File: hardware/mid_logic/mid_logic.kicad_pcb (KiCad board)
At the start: 4 copper layers, 52 x 52 mm, 52 parts, among them J2 J_STK_A, J3 J_STK_B, J4 RS485 A/B/GND, J5 Feld: 4 Reed, J6 Haubenkontakt, J7 USB-C, Q2 BC847, SW1 RESET, SW2 BOOT, U1 ESP32-S3-WROOM-1-N16R8, U2 MAX3485, U3 PCF8575, U4 PhotoMOS 60V, U5 USBLC6-2SC6

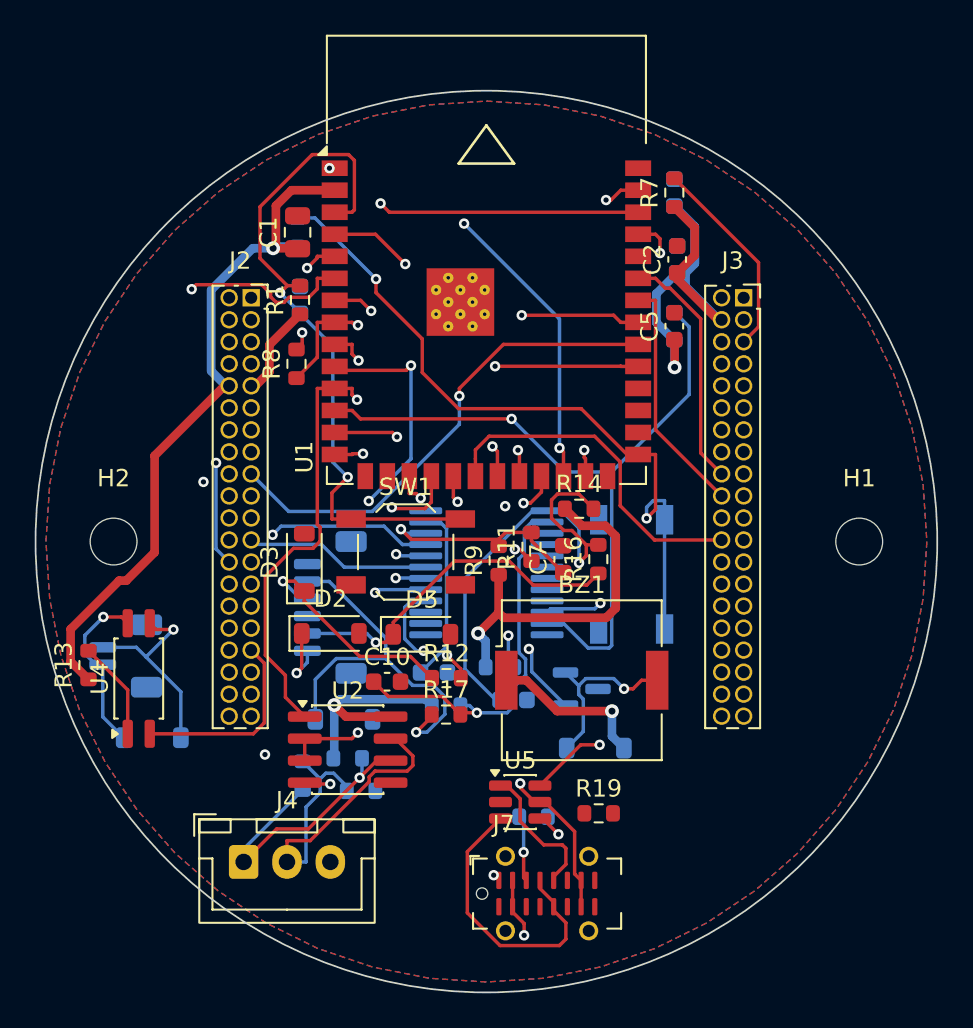
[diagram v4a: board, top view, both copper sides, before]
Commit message: docs/16: Anleitung fuer die letzten Handgriffe in KiCad
Was der Autorouter uebrig laesst, ist wenig und immer dasselbe Muster: Pads,
die zwischen anderen Bauteilen eingeklemmt sind. Die Anleitung nennt die
Tastenkuerzel (X fuer Bahn, V fuer Lagenwechsel mit Via, B fuer Zonen
fuellen), den aktuellen Stand je Board als Anhaltspunkt und die
Reihenfolge danach - Zonen fuellen VOR der DRC, sonst sucht man Fehler, die
keine sind.

Dazu zwei Warnungen: keine Bauteile verschieben, die Positionen kommen aus
gen_layouts.py und gehen beim naechsten Neuerzeugen verloren. Und die Regeln
nicht lockern - wenn die DRC meckert, ist die Bahn falsch.

Co-Authored-By: Claude Opus 5 (1M context) <noreply@anthropic.com>
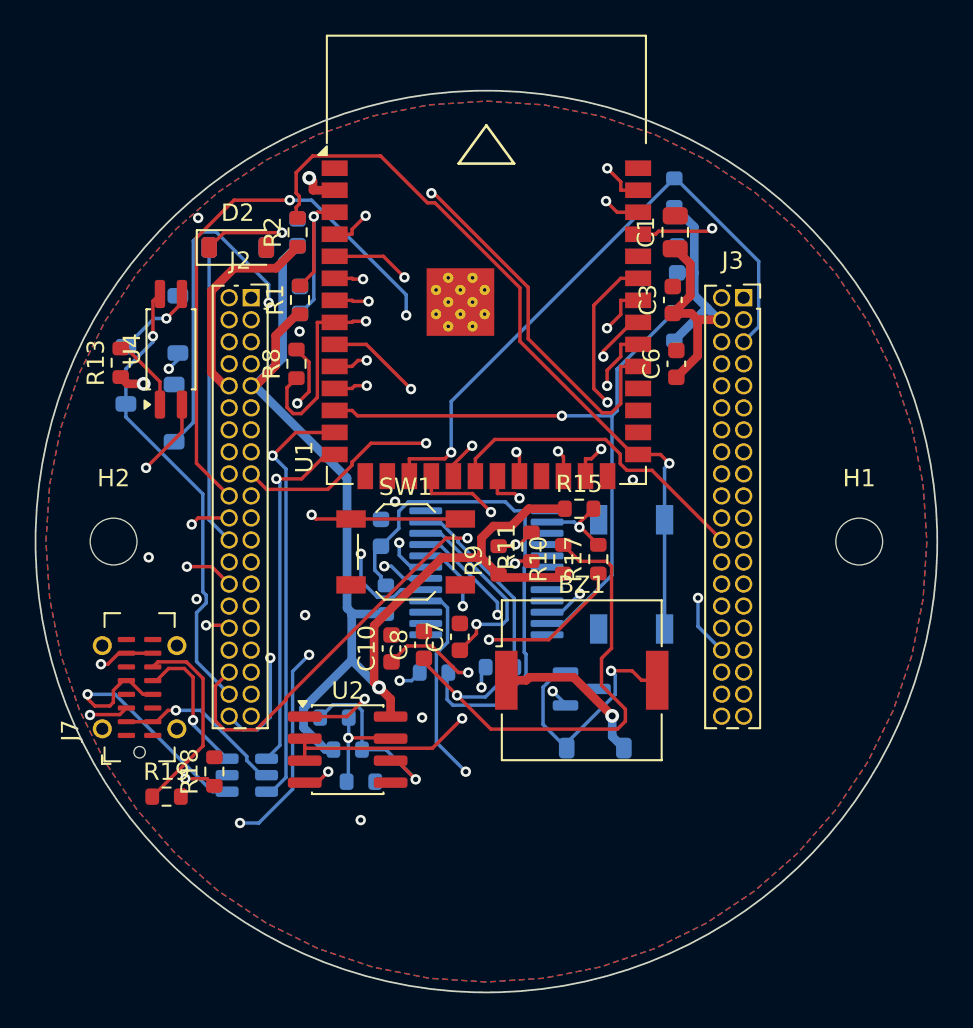
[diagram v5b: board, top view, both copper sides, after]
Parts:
- removed J4: RS485 A/B/GND, JST_XH_B3B-XH-A_1x03_P2.50mm_Vertical
- removed J5: Feld: 4 Reed, JST_SH_BM06B-SRSS-TB_1x06-1MP_P1.00mm_Vertical
- removed J6: Haubenkontakt, JST_SH_BM02B-SRSS-TB_1x02-1MP_P1.00mm_Vertical
- C2, C5, D3, D5, R12, R14, R16, R7, U5: moved to B.Cu
- C3, C6, C8, R10, R15, R18, R2: moved to F.Cu
- moved J7 26.3 mm to (-20.0, 8.40), turned to 90 degrees
- moved R19 24.9 mm to (-18.4, 14.7)
- moved D2 22.9 mm to (-14.3, -17.0)
- moved D5 22.7 mm to (-17.8, -12.5), turned to 90 degrees
- moved C5 22.4 mm to (-10.9, -17.8)
- moved C1 21.8 mm to (10.9, -17.8)
- moved D4 21.0 mm to (-20.8, -9.59), turned to 90 degrees
- moved D6 20.2 mm to (-18.0, -7.41), turned to 90 degrees
- moved U4 19.1 mm to (-18.2, -11.1)
- moved R18 18.6 mm to (-15.7, 13.3), turned to 90 degrees
- moved D3 18.6 mm to (-14.3, -17.0), turned to 0 degrees
- moved R13 17.5 mm to (-21.1, -10.3)
- moved U5 15.8 mm to (-13.8, 13.5)
- moved R15 13.7 mm to (5.35, -1.89)
- moved R17 12.5 mm to (6.45, 1.02), turned to 90 degrees
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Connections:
- J2 pad 24: RSV_A2 -> REED2_IN
- J2 pad 25: PGND -> SAB2_IN
- J2 pad 34: RSV_A3 -> RS485_A
- J2 pad 35: RSV_A4 -> RS485_B
- J2 pad 36: RSV_A5 -> REED1_IN
- J2 pad 37: RSV_A6 -> SAB1_IN
- J2 pad 38: PGND -> HOOD_A
- J2 pad 39: PGND -> HOOD_B
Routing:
- net RELAY_CTL: track 28.0 -> 67.6 mm, vias 1 -> 4
- net REED2_IN: track 13.1 -> 50.7 mm
- net SAB2_IN: track 22.7 -> 59.1 mm, vias 1 -> 3
- net USB_VBUS: track 58.3 -> 32.6 mm
- net QSPI_D3: track 25.7 -> 0.00 mm, vias 1 -> 0
- net EXP_P7: track 18.3 -> 41.7 mm, vias 2 -> 1
- net HW_TRIP1: track 26.5 -> 49.7 mm, vias 1 -> 2
- net HOOD_B: track 12.0 -> 31.9 mm
- net SAB1_IN: track 20.2 -> 39.1 mm, vias 1 -> 2
- net REED1_IN: track 36.1 -> 53.5 mm, vias 3 -> 4
- net HOOD_A: track 10.1 -> 26.8 mm
- net M2_INB: track 47.1 -> 63.4 mm
- net TRIP_RST: track 22.0 -> 37.8 mm, vias 1 -> 3
- net I2C_SCL: track 63.9 -> 50.1 mm
- net USB_CC2: track 0.00 -> 11.4 mm
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
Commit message: Endstand nach dem Umbau: 13 offene Signale, 23 Masse-Inseln, ein Haarriss
Alle drei Boards mit der integrierten Bruecke, dem gemeinsamen Feldstecker,
der quergestellten USB-Buchse und den zusammengelegten Frontsensoren neu
erzeugt und geroutet.

              Bauteile  Segmente  offene Signale  Masse-Inseln  Kupferfehler
  top_ui         20        149          3               1            0
  mid_logic      47        795          3              12            1
  bottom         79        768          7              10            0

Bottom hat 23 Bauteile weniger als vorher und zum ersten Mal null
Kupferfehler. Auf Top haengen alle drei offenen Netze am selben Bauteil - dem
Raumsensor, der gerade neben den ToF gewandert ist; der Router kam zwischen
ihm und dem Ecktaster nicht mehr heraus.

MITERZEUGT: Nutzen (173,4 x 72,4 mm, deckungsgleich mit der Summe der
Einzelboards), Bestellunterlagen fuer alle vier, 3D-Renderings und die
STEP-Baugruppe. Die misst jetzt 70 x 72,3 x 39,6 mm - sie ist gewachsen, weil
die Klinkenbuchse mittig sitzt und ihr Modell nach hinten ragt.

Die Stueckliste ist von 46 auf 42 Positionen geschrumpft (Bottom) bzw. von 28
auf 25 (Mid). Ohne LCSC-Nummer sind weiterhin alle - das bleibt der naechste
Schritt vor der Bestellung.

docs/13 und docs/16 auf die Endzahlen.

Co-Authored-By: Claude Opus 5 (1M context) <noreply@anthropic.com>
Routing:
- net PGND: track 0.00 -> 21.0 mm, vias 0 -> 1
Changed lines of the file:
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@@
+	)
+	(segment
+		(start -1.530734 4.720518)
+		(end -3.262784 3.720518)
+		(width 0.4)
+		(layer "F.Cu")
+		(net "PGND")
+	)
+	(segment
+		(start -1.530734 4.720518)
+		(end -3.262784 3.720518)
+		(width 0.4)
+		(layer "F.Cu")
+		(net "PGND")
+	)
+	(segment
+		(start -17.85 10.8)
+		(end -18.238228 12.248888)
+		(width 0.4)
+		(layer "F.Cu")
+		(net "PGND")
+	)
+	(segment
+		(start -17.85 10.8)
+		(end -18.238228 12.248888)
+		(width 0.4)
+		(layer "F.Cu")
+		(net "PGND")
+	)
+	(segment
+		(start -1.530734 4.720518)
+		(end -3.262784 3.720518)
+		(width 0.4)
+		(layer "F.Cu")
+		(net "PGND")
+	)
+	(segment
+		(start -1.530734 4.720518)
+		(end -3.262784 3.720518)
+		(width 0.4)
+		(layer "F.Cu")
+		(net "PGND")
+	)
+	(segment
+		(start -22.15 6)
+		(end -23.387436 7.237436)
+		(width 0.4)
+		(layer "F.Cu")
+		(net "PGND")
+	)
+	(segment
+		(start -22.15 6)
+		(end -23.387436 7.237436)
+		(width 0.4)
+		(layer "F.Cu")
+		(net "PGND")
+	)
+	(segment
+		(start -17.85 10.8)
+		(end -18.238228 12.248888)
+		(width 0.4)
+		(layer "F.Cu")
+		(net "PGND")
+	)
+	(segment
+		(start -22.15 6)
+		(end -23.387436 7.237436)
+		(width 0.4)
+		(layer "F.Cu")
+		(net "PGND")
+	)
+	(segment
+		(start -17.85 10.8)
+		(end -18.238228 12.248888)
+		(width 0.4)
+		(layer "F.Cu")
+		(net "PGND")
+	)
+	(segment
+		(start -22.15 6)
+		(end -23.387436 7.237436)
+		(width 0.4)
+		(layer "F.Cu")
+		(net "PGND")
+	)
+	(via
+		(at 10.448616 -14.706782)
+		(size 0.6)
+		(drill 0.3)
+		(layers "F.Cu" "B.Cu")
+		(net "PGND")
 	)
 	(segment

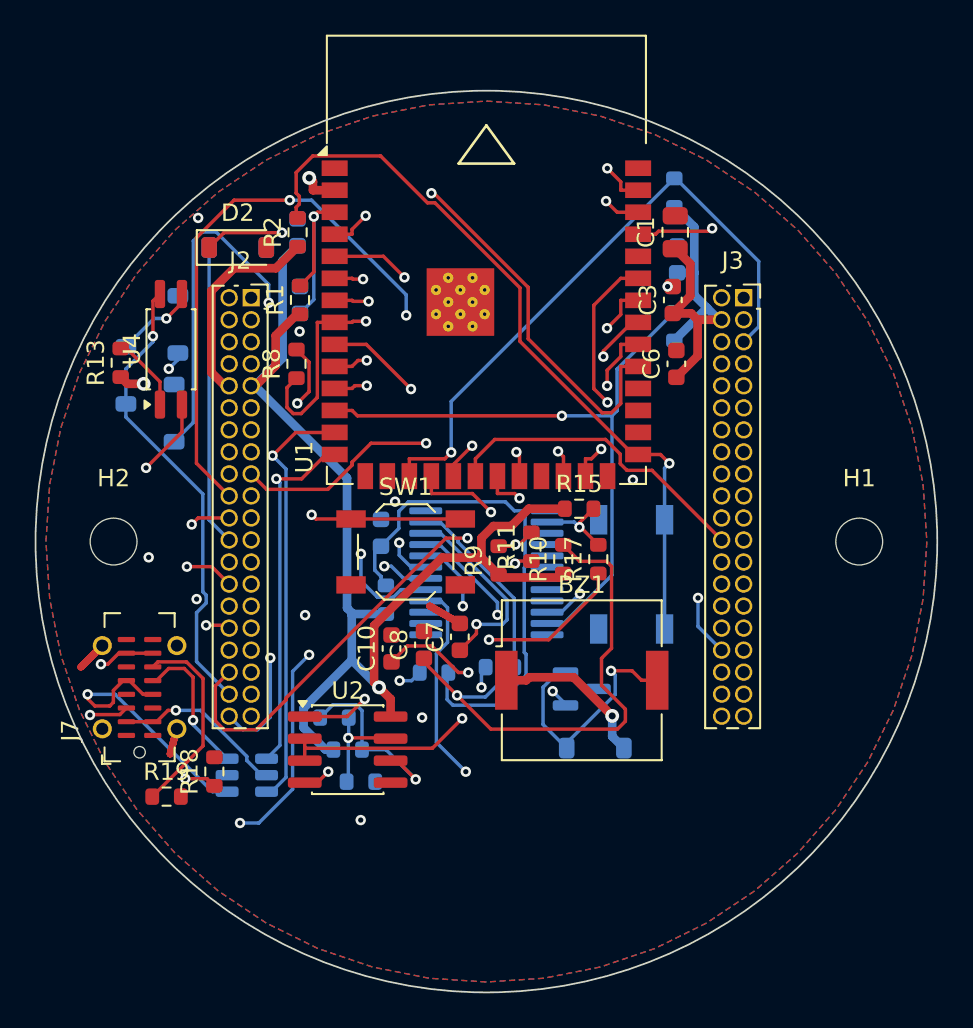
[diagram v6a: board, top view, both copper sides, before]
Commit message: docs/17: woher die Daten der vier offenen Bauteile kommen
Display, Klinkenbuchse, USB-C und Feldstecker blockieren die Bestellung -
jedes aus einem anderen Grund. Die Seite sagt je Teil, was genau fehlt, wo es
herkommt und was davon abhaengt.

DISPLAY ist der kritische Fall: Im Schaltplan steht ein Platzhalter, ein
1,27-mm-Stiftleisten-Footprint mit zehn Pins und dem Vermerk PLATZHALTER. Es
ist weder ein Bauteil gewaehlt noch ein Anschluss festgelegt.

Dabei faellt eine Bauform schon raus: Die verbreiteten Fertigmodule mit
Traegerplatine messen 48 x 31 mm - einen Millimeter breiter als unser
Top-Board. Es muss ein nacktes Panel mit FPC-Fahne sein, rund 30 x 36 mm.
Kandidaten bei buydisplay.com (ER-TFT1.69-1), Datenblaetter dort nur im
Browser, automatische Downloads blockt der Anbieter.

Fuenf Zahlen sind aus dem Datenblatt zu holen, und eine davon ist die
entscheidende: die Lage der AKTIVEN Flaeche im Aussenmass. Das Fenster der
Zentralscheibe misst 32,7 x 27,0 und liegt bei (-0,95 / +0,3) - ein Panel mit
asymmetrischem Rand verschiebt das Bild darin.

SCHRAUBKLEMMEN STATT STECKVERBINDER geprueft und verworfen. Sie sind
einreihig, sechzehn Pole werden dadurch doppelt so lang:

  Schraubklemme 3,5 mm   56,0 mm   passt nicht auf Durchmesser 52
  Schraubklemme 2,54 mm  40,6 mm   passt, aber winzig
  Micro-Fit 3.0 2x8      28,15 mm  passt

Dazu entfiele der vorbereitete Kabelbaum mit einem Klick - bei Schraubklemmen
wird in der Dose geschraubt, einzeln, ueber Kopf. Empfehlung: Micro-Fit
behalten, das STEP-Modell gibt es bei Molex zu jeder Bestellnummer.

Co-Authored-By: Claude Opus 5 (1M context) <noreply@anthropic.com>
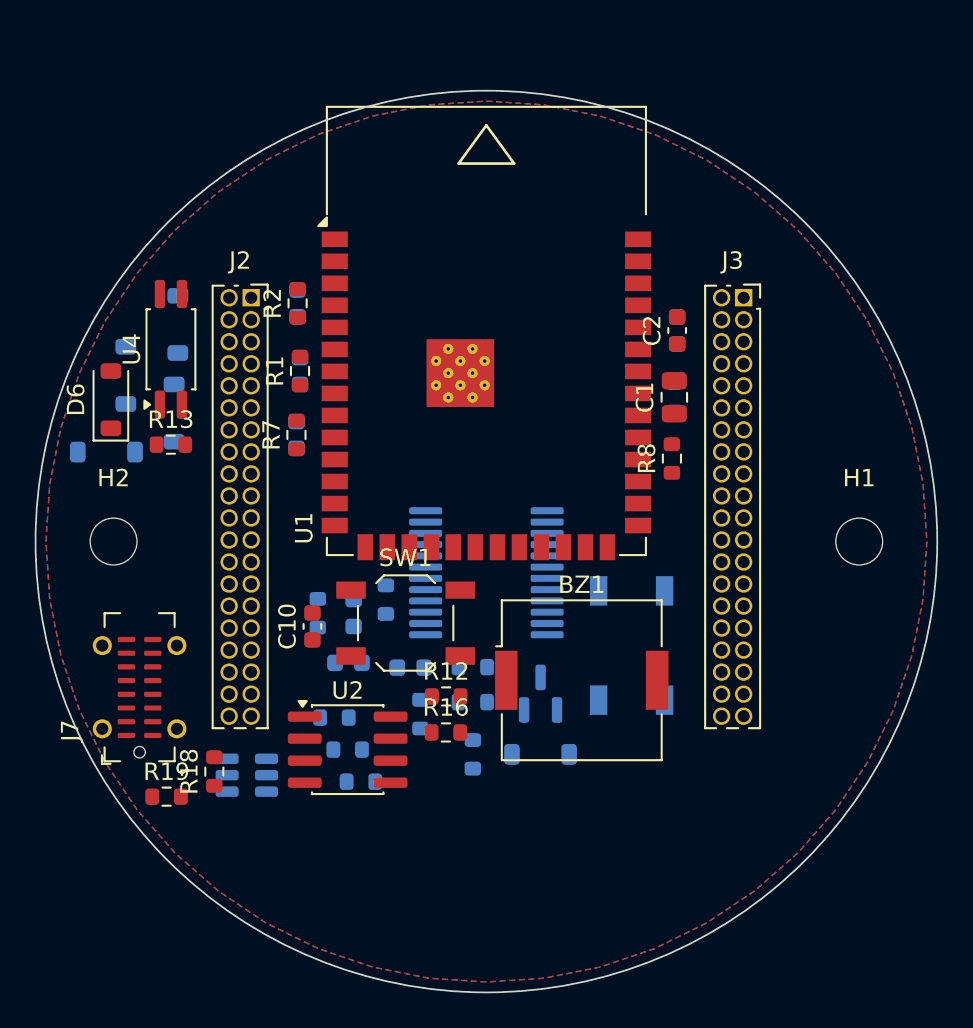
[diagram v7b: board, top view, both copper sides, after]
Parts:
- C2, D6, R12, R16, R7: moved to F.Cu
- C3, C6, C7, C8, D2, R10, R11, R15, R17, R9: moved to B.Cu
- moved R7 25.9 mm to (-11.0, -6.15)
- moved R8 22.3 mm to (10.7, -4.79)
- moved C6 22.3 mm to (-11.0, -6.15)
- moved R15 16.2 mm to (-9.72, 4.13), turned to 90 degrees
- moved R17 13.4 mm to (-0.78, 12.3)
- moved D3 10.2 mm to (-18.0, -7.41), turned to 90 degrees
- moved R10 9.75 mm to (-0.78, 9.26), turned to 0 degrees
- moved C1 9.52 mm to (10.8, -8.32)
- moved R11 8.93 mm to (-5.80, 3.35)
- moved C9 7.73 mm to (-7.95, 7.00), turned to 0 degrees
- moved R14 6.90 mm to (-3.80, 9.96)
- moved R9 6.33 mm to (-0.78, 7.24), turned to 0 degrees
- moved D2 5.62 mm to (-17.8, -12.5), turned to 90 degrees
- moved R13 5.54 mm to (-18.2, -5.59), turned to 0 degrees
- moved C10 4.73 mm to (-10.0, 4.89)
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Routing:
- net 3V3_SYS: track 159.3 -> 0.00 mm, vias 3 -> 0
- net RELAY_CTL: track 67.6 -> 0.00 mm, vias 4 -> 0
- net M2_INB: track 63.4 -> 0.00 mm, vias 3 -> 0
- net I2C_SDA: track 63.0 -> 0.00 mm, vias 1 -> 0
- net SAB2_IN: track 59.1 -> 0.00 mm, vias 3 -> 0
- net AUDIO_PWM: track 55.6 -> 0.00 mm, vias 1 -> 0
- net REED1_IN: track 53.5 -> 0.00 mm, vias 4 -> 0
- net M2_INA: track 51.9 -> 0.00 mm, vias 3 -> 0
- net I_SENSE2: track 51.3 -> 0.00 mm, vias 3 -> 0
- net UART485_TX: track 50.8 -> 0.00 mm, vias 2 -> 0
- net REED2_IN: track 50.7 -> 0.00 mm, vias 1 -> 0
- net I2C_SCL: track 50.1 -> 0.00 mm, vias 2 -> 0
- net HW_TRIP1: track 49.7 -> 0.00 mm, vias 2 -> 0
- net UART485_RX: track 46.1 -> 0.00 mm, vias 2 -> 0
- net I_SENSE1: track 45.9 -> 0.00 mm, vias 1 -> 0
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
